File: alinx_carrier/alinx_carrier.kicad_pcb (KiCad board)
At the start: 2 copper layers, 4 parts, among them J1 AXK6A2337YG, J2 AXK6A2337YG, J3 AXK6A2337YG, J4 AXK6A2337YG

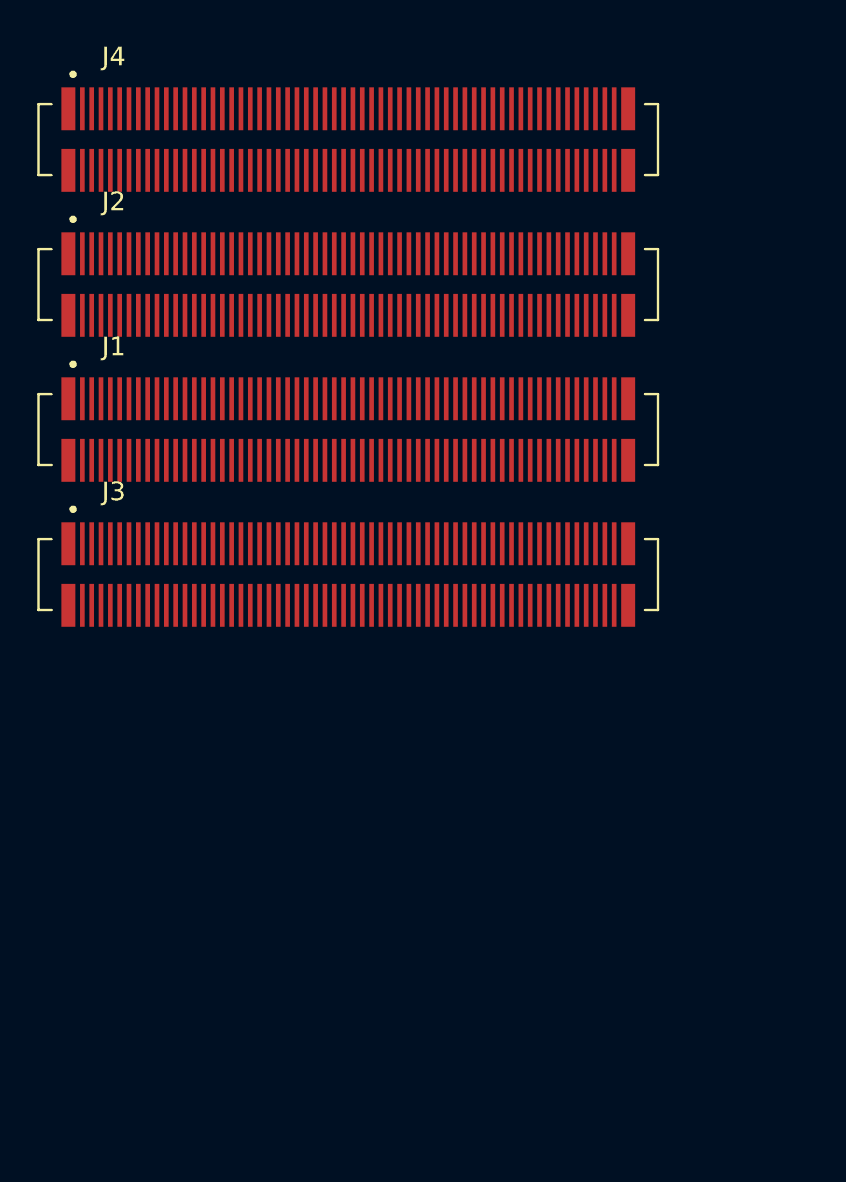
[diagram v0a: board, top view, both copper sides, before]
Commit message: pulled in latest files froms snapeda for AXK6A2337YG
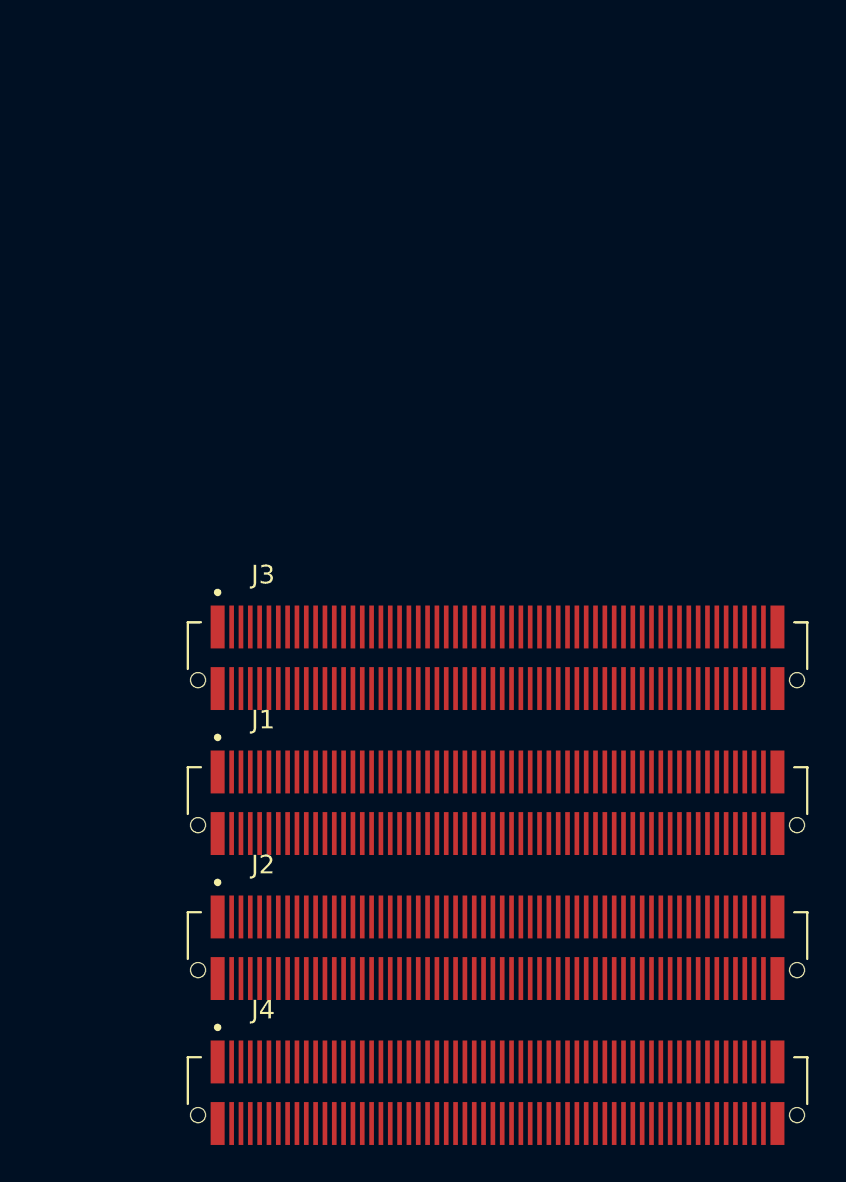
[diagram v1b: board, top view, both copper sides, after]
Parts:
- moved J4 51.7 mm to (94.0, 118.5)
- moved J2 36.4 mm to (94.0, 110.8)
- moved J1 21.5 mm to (94.0, 103.0)
- moved J3 9.16 mm to (94.0, 95.2)

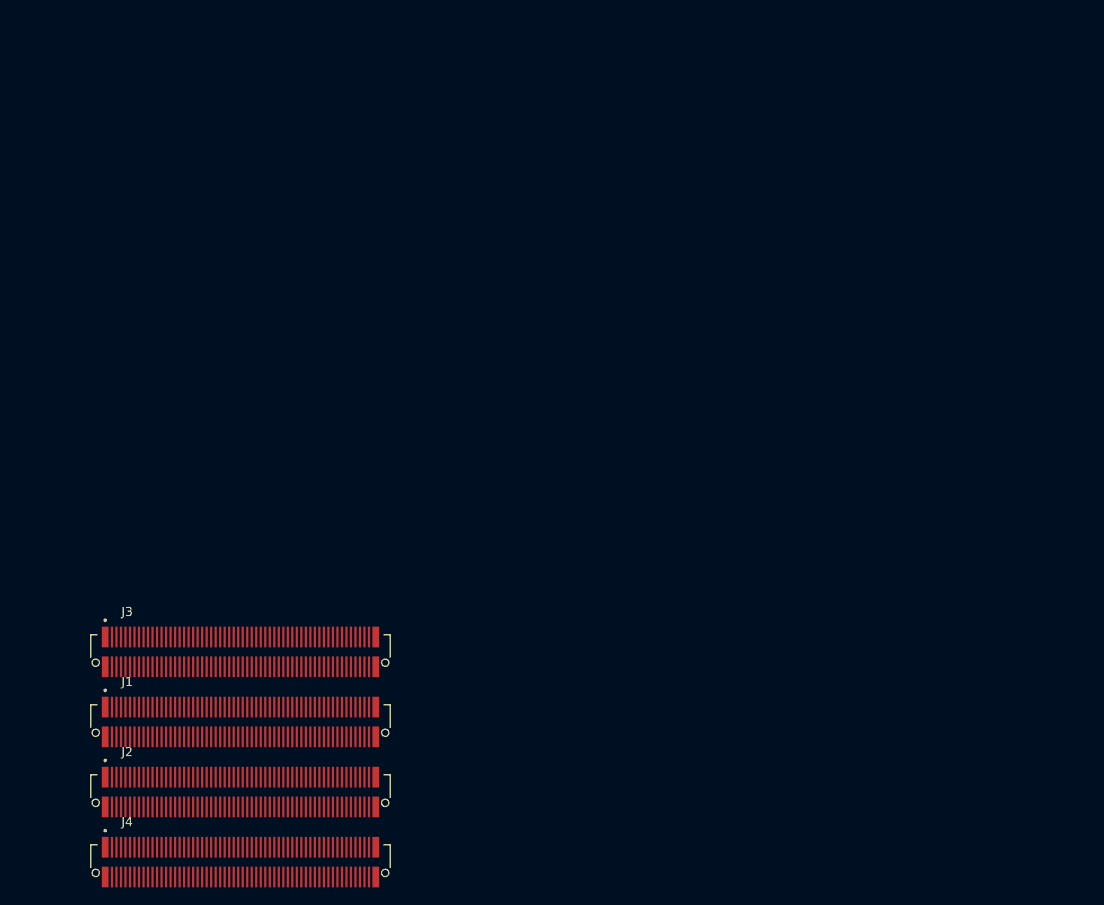
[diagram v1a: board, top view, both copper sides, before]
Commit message: added mounting holes to alinx carrier
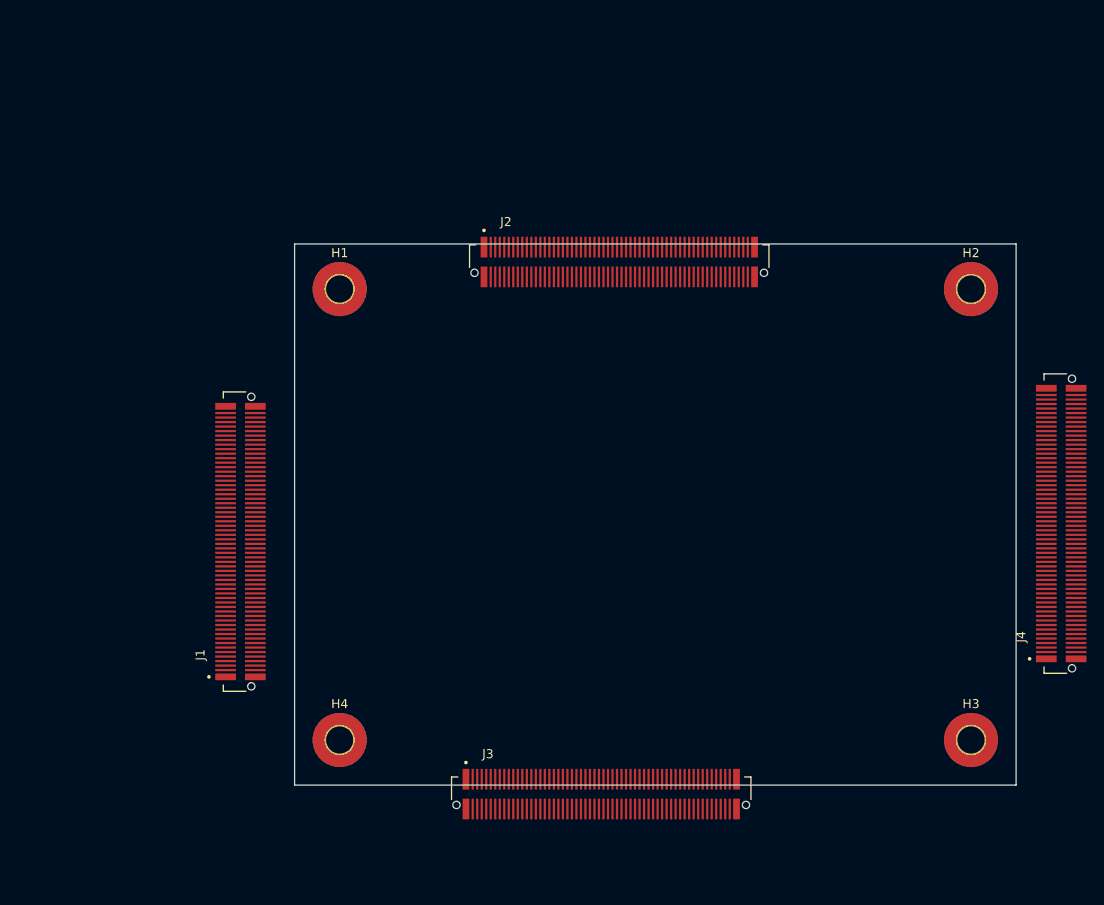
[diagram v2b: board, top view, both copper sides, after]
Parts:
- added H1: MountingHole_Pad, MountingHole:MountingHole_3mm_Pad_TopBottom, F.Cu at (105.0, 55.0)
- added H2: MountingHole_Pad, MountingHole:MountingHole_3mm_Pad_TopBottom, F.Cu at (175.0, 55.0)
- added H3: MountingHole_Pad, MountingHole:MountingHole_3mm_Pad_TopBottom, F.Cu at (175.0, 105.0)
- added H4: MountingHole_Pad, MountingHole:MountingHole_3mm_Pad_TopBottom, F.Cu at (105.0, 105.0)
- moved J4 98.4 mm to (185.0, 81.0), turned to 90 degrees
- moved J2 72.2 mm to (136.0, 52.0)
- moved J3 43.0 mm to (134.0, 111.0)
- moved J1 20.0 mm to (94.0, 83.0), turned to 90 degrees
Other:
- board outline added: 80 x 60 mm

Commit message: created dimensioned drawing. Connector locations are questionable.
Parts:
- moved J1 10.2 mm to (103.8, 80.0), turned to -90 degrees
- moved J4 8.82 mm to (176.2, 80.0)
- moved J3 7.66 mm to (140.0, 106.2)
- moved J2 4.37 mm to (140.0, 53.8), turned to 180 degrees
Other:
- board outline removed

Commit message: alinx carrier dimensions work
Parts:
- added J5: HR911130A, pedrolib:HANRUN_HR911130A, F.Cu at (168.0, 39.0)
- added U1: KSZ9031RNXCA, Package_DFN_QFN:QFN-48-1EP_7x7mm_P0.5mm_EP5.15x5.15mm, F.Cu at (134.4, 36.6)

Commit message: put some usb-c stuff on the alinx carrier
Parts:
- added J6: USB4105-GF-A, pedrolib:GCT_USB4105-GF-A, F.Cu at (102.5, 35.0)
- added U2: STUSB4500QTR, Package_DFN_QFN:QFN-24-1EP_4x4mm_P0.5mm_EP2.7x2.7mm, F.Cu at (117.0, 35.0)
- moved U1 12.8 mm to (147.0, 35.0)
- moved J5 4.14 mm to (169.1, 35.0)
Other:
- board outline added: 80 x 85 mm

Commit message: added jtag connector
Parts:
- added J7: 87832-1420, pedrolib:MOLEX_87832-1420, F.Cu at (131.0, 37.0)
